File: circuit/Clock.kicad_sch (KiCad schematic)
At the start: 15 parts, among them U2 Max98357

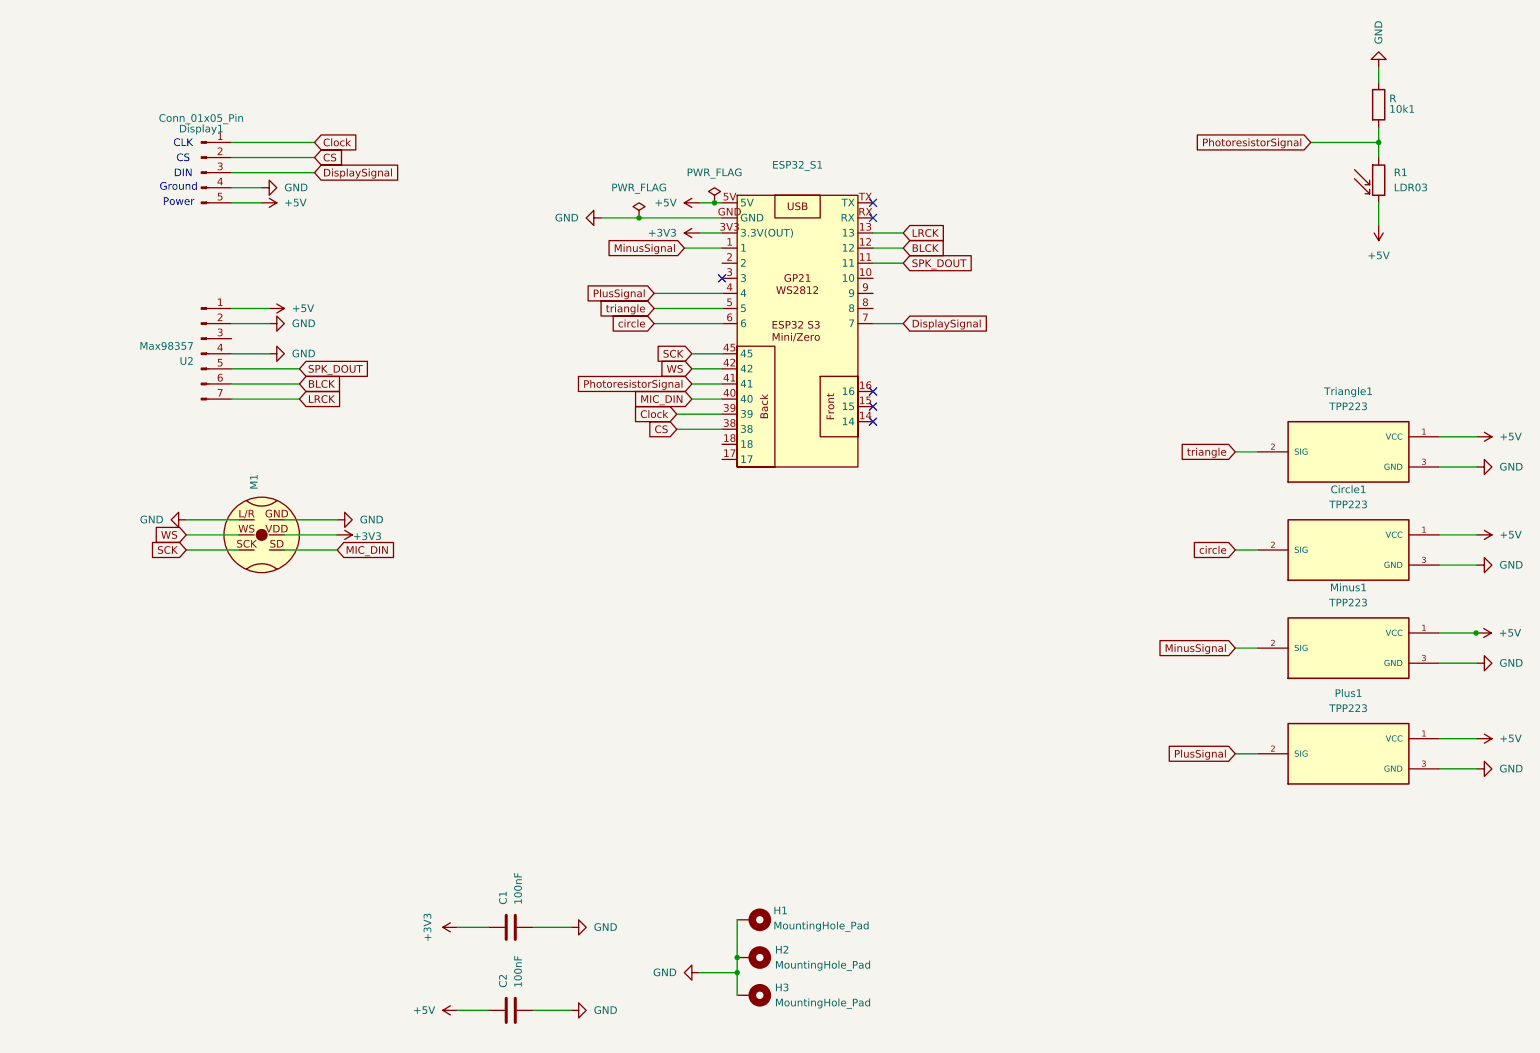
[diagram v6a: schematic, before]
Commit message: switched to mom-switches rather than ttp223 capacitive sensors
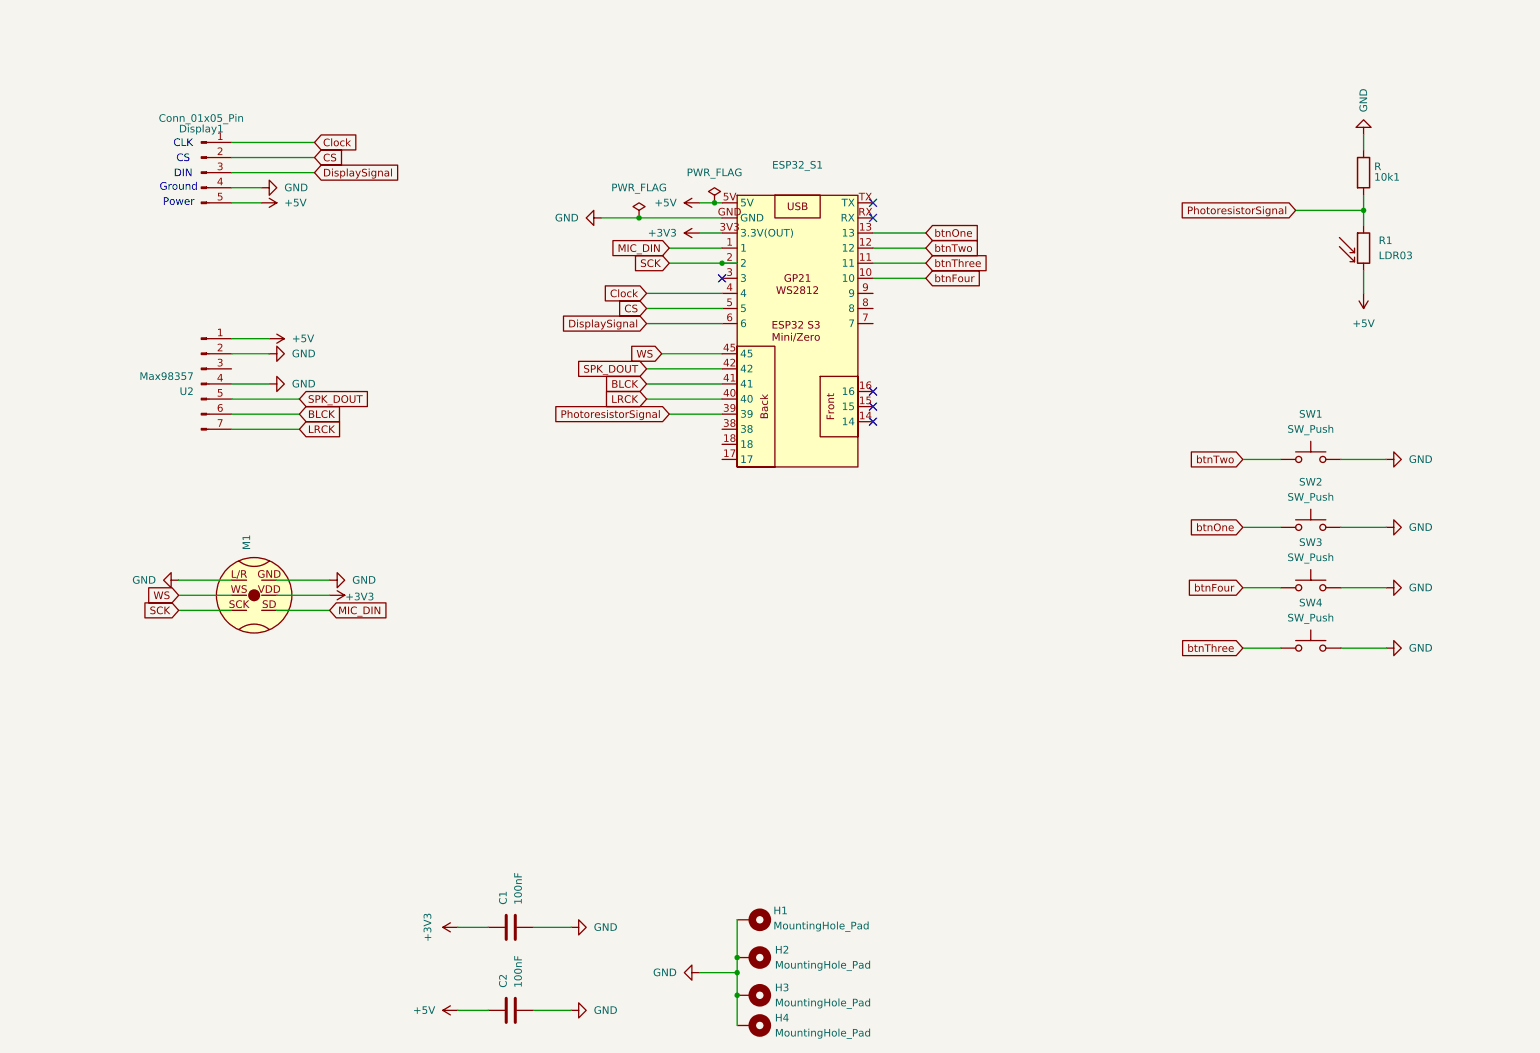
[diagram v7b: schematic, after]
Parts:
- removed Circle1, Minus1, Plus1, Triangle1: TPP223, Connector_PinHeader_2.54mm:PinHeader_1x03_P2.54mm_Vertical, symbol PaulsCoolKicadLibrary:TPP223
- added H4: MountingHole_Pad, MountingHole:MountingHole_3.2mm_M3_Pad, symbol Mechanical:MountingHole_Pad
- added SW1, SW2, SW3, SW4: SW_Push, Button_Switch_THT:SW_PUSH_6mm_H5mm, symbol Switch:SW_Push
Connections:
- net MinusSignal is gone; now on net MIC_DIN: ESP32_S1.1
- net PlusSignal is gone; now on net Clock: ESP32_S1.4
- net circle is gone; now on net DisplaySignal: ESP32_S1.6
- net triangle is gone; now on net CS: ESP32_S1.5
- net BLCK: now also ESP32_S1.41; no longer ESP32_S1.12
- net CS: no longer ESP32_S1.38
- net Clock: no longer ESP32_S1.39
- net DisplaySignal: no longer ESP32_S1.7
- net GND: now also H4.1, SW1.2, SW2.2, SW3.2, SW4.2
- net LRCK: now also ESP32_S1.40; no longer ESP32_S1.13
- net MIC_DIN: no longer ESP32_S1.40
- net PhotoresistorSignal: now also ESP32_S1.39; no longer ESP32_S1.41
- net SCK: now also ESP32_S1.2; no longer ESP32_S1.45
- net SPK_DOUT: now also ESP32_S1.42; no longer ESP32_S1.11
- net WS: now also ESP32_S1.45; no longer ESP32_S1.42
- net btnFour: now reaches ESP32_S1.10
- net btnFour: now also SW3.1
- new net btnOne: ESP32_S1.13, SW2.1
- new net btnThree: ESP32_S1.11, SW4.1
- new net btnTwo: ESP32_S1.12, SW1.1
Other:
- moved on the sheet: 10k1, M1, R1, U2

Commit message: fully functional based on breadboard prototype
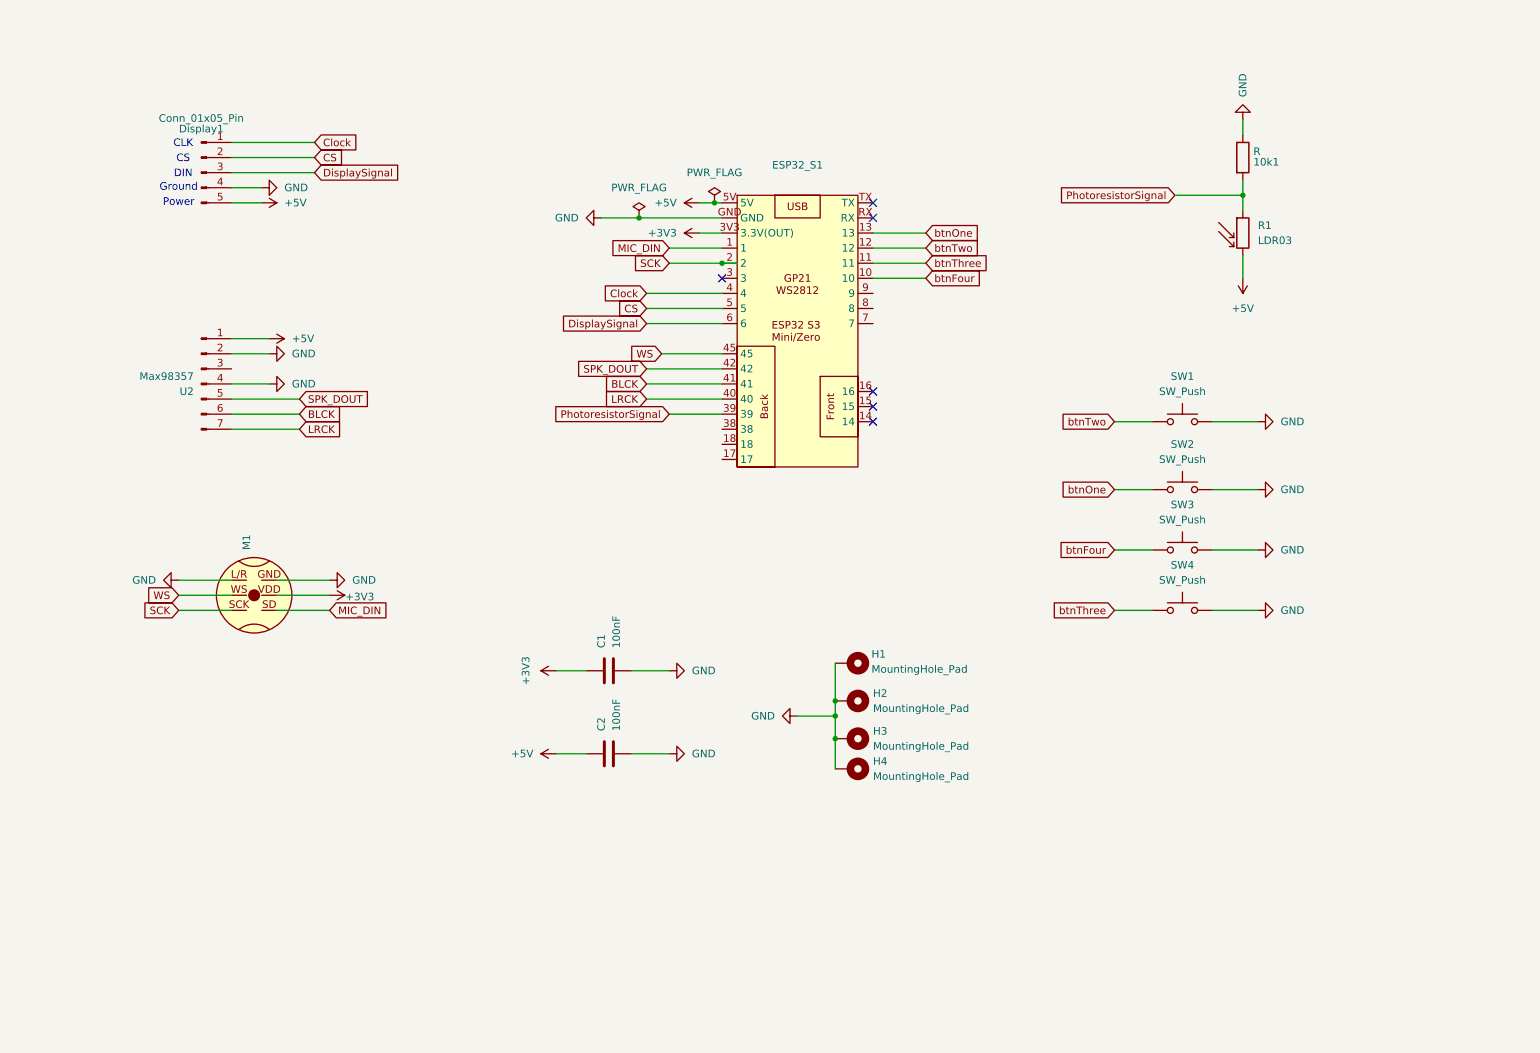
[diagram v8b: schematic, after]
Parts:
- R1: footprint OptoDevice:R_LDR_10x8.5mm_P7.6mm_Vertical -> OptoDevice:R_LDR_4.9x4.2mm_P2.54mm_Vertical
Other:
- moved on the sheet: 10k1, C1, C2, H1, H2, H3, H4, R1, SW1, SW2, SW3, SW4
